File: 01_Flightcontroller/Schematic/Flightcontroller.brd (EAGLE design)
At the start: 63.5 x 61.9 mm, 89 parts, among them IC1 FT232RL, IC2 MPU6000, IC3 BMP280, J1 2908-05WB-MG, U1 STM32F7X2RXT, U2 ATMEGA328P_TQFP, U3 LM3940IMPX-3.3/NOPB, U4 TXB0104, Y1 8MHz, Y2 16MHz

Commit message: Richtiges routen hilfe durch bruno
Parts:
- moved GY87 29.2 mm to (19.1, 91.4)
- moved SONIC1 29.2 mm to (39.4, 99.1)
- moved SONIC2 29.2 mm to (39.4, 96.5)
- moved C34 12.0 mm to (-3.81, 64.8), turned to 90 degrees
- moved ISP1 10.2 mm to (52.1, 64.8)
- moved GPS 10.2 mm to (12.7, 99.1)
- moved OSD 10.2 mm to (12.7, 96.5)
- moved C4 8.98 mm to (39.4, 80.0), turned to 90 degrees
- moved C3 8.89 mm to (27.9, 86.4)
- moved LED_STRIPES 8.89 mm to (29.2, 99.1)
- moved C23 8.52 mm to (-1.27, 64.8), turned to 90 degrees
- moved R2 8.03 mm to (49.5, 86.4)
- moved R3 8.03 mm to (49.5, 83.8)
- moved U4 7.41 mm to (49.5, 77.5)
- moved C28 7.41 mm to (54.6, 80.0)
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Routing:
- net GND: track 264.3 -> 570.1 mm, vias 6 -> 7
- net TRIGG1_IN: track 94.5 -> 21.4 mm, vias 3 -> 0
- net VCC: track 289.1 -> 332.4 mm, vias 13 -> 12
- net ECHO1_IN: track 79.3 -> 40.7 mm, vias 2 -> 0
- net VCC_2: track 207.6 -> 245.9 mm
- net TRIGG2_IN: track 48.6 -> 11.7 mm, vias 3 -> 0
- net UART1_TX: track 92.1 -> 59.1 mm, vias 4 -> 2
- net I2C2_SDA: track 65.3 -> 35.4 mm, vias 1 -> 4
- net UART2_TX: track 59.4 -> 30.3 mm
- net SPI2_MISO: track 76.8 -> 47.8 mm, vias 4 -> 1
- net SD1_CK: track 70.2 -> 43.3 mm, vias 5 -> 1
- net LED_TX: track 50.3 -> 24.1 mm, vias 0 -> 2
- net SD1_CMD: track 62.8 -> 37.2 mm, vias 5 -> 1
- net ECHO2_IN: track 33.3 -> 12.4 mm, vias 2 -> 1
- net A_SPI_NSS: track 47.2 -> 27.7 mm, vias 3 -> 1
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- removed copper zone on layer 16, net GND

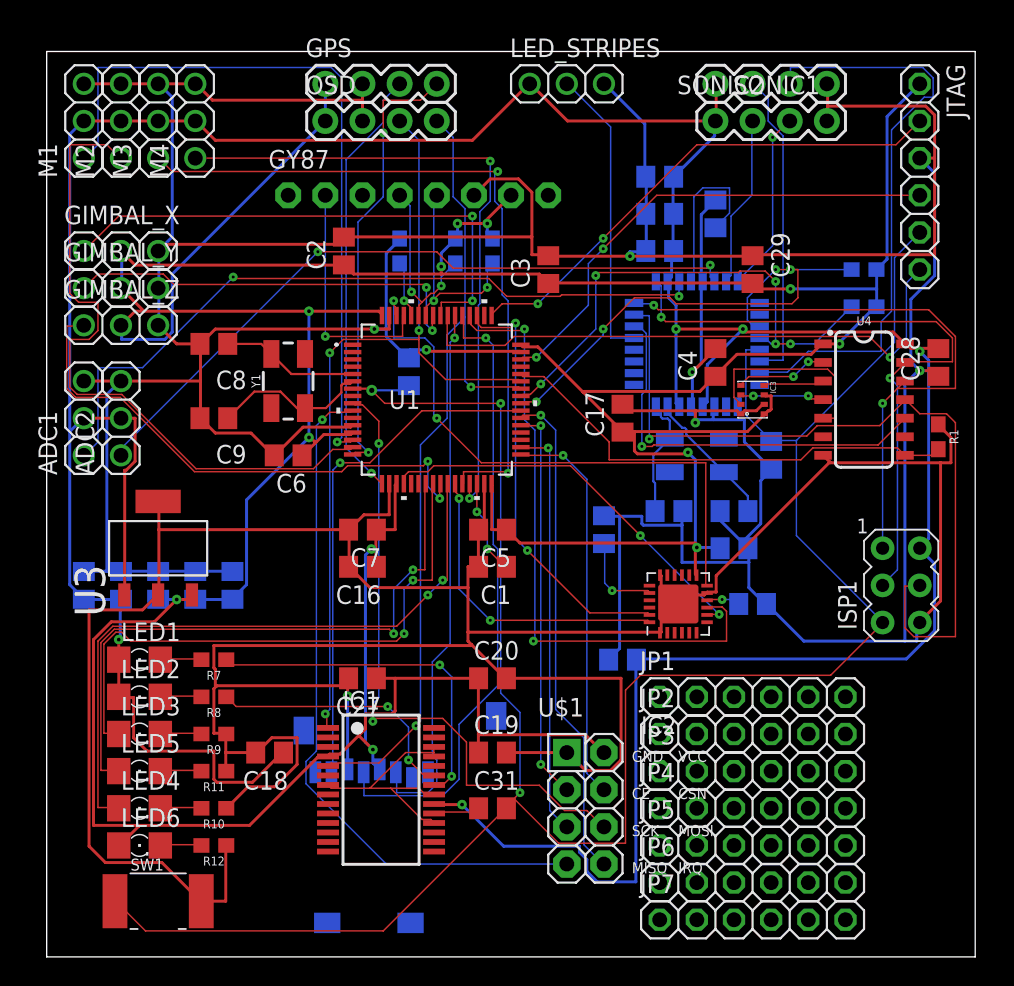
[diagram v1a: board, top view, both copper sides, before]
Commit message: Hinzufügen USB , BATTSENS und VCC/GNDLAYER
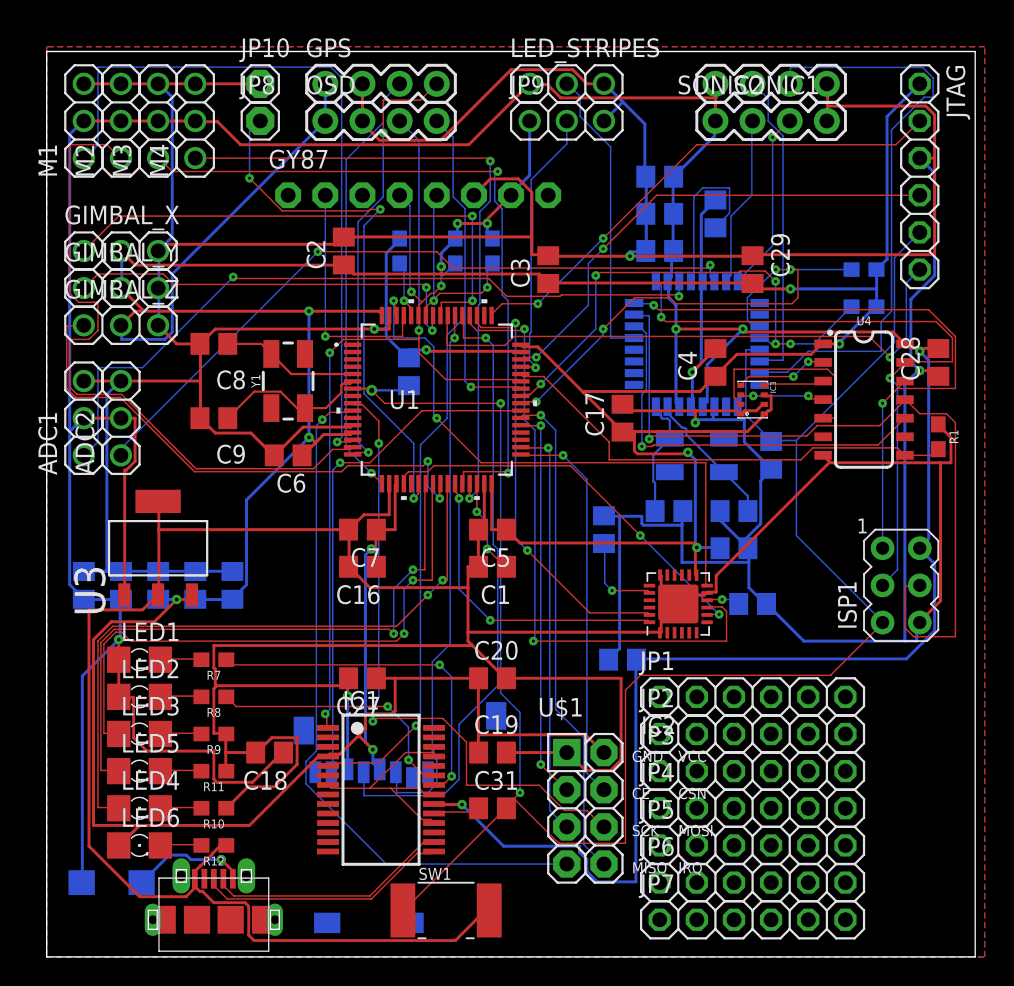
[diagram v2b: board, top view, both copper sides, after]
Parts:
- added D1: (no value), diode:DO214BA
- added JP10, JP8: (no value), adafruit:1X01
- added JP9: (no value), adafruit:1X03
- added U$2: MICRO-USB-RECEPTACLE47589-0001, con-molex-usb:47589-0001
- moved SW1 19.7 mm to (21.0, 42.5)
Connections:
- new net USBDM: IC1.16, U$2.4
- new net USBDP: IC1.15, U$2.3
- new net V_USB: D1.A, U$2.5
- net BATTSENS: now also JP8.1
- net GND: now also JP10.1, JP9.3, U$2.1
- net USBOSD: now also JP9.2
- net VCC: now also JP9.1
- net VCC_2: now also D1.C
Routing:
- net BATTSENS: track 0.00 -> 36.9 mm, vias 0 -> 3
- net GND: track 570.1 -> 605.8 mm
- net RST: track 155.0 -> 133.9 mm
- net USBOSD: track 0.00 -> 19.1 mm, vias 0 -> 1
- net VCC_2: track 245.9 -> 264.2 mm
- net USBDM: track 0.00 -> 17.4 mm
- net USBDP: track 0.00 -> 17.2 mm
- net V_USB: track 0.00 -> 7.99 mm, vias 0 -> 1
- net VCC: track 332.4 -> 337.9 mm
- added copper zone on layer 16, net GND
- added copper zone on layer 1, net VCC

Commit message: Finnishing Board up. BOM
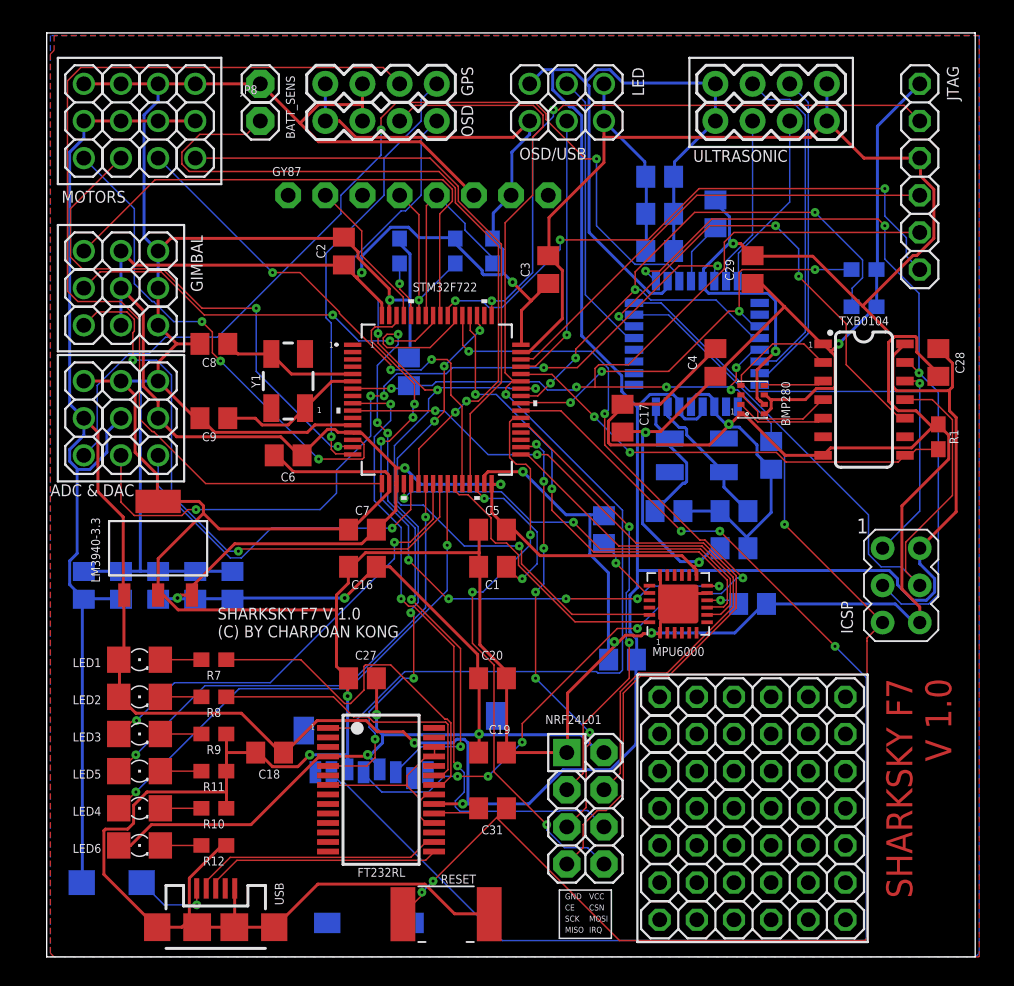
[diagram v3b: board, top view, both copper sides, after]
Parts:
- removed SW1: (no value), adafruit:BTN_CK_KSS
- removed U$2: MICRO-USB-RECEPTACLE47589-0001, con-molex-usb:47589-0001
- added DAC: (no value), adafruit:1X03
- added RESET: (no value), adafruit:BTN_CK_KSS
- added USB: (no value), SparkFun-Connectors:USB-MICROB
- C23: value 1uF -> 10uF
- renumbered IC1 to FT232RL, IC2 to MPU6000, IC3 to BMP280, ISP1 to ICSP, J1 to SD_CARD, JP10 to BATT_SENS, JP9 to OSD/USB, LED_STRIPES to LED, U$1 to NRF24L01, U1 to STM32F722, U2 to ATMEGA328P, U3 to LM3940-3.3, U4 to TXB0104
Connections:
- net DAC_OUT: now also DAC.1
- net GND: now also DAC.3, RESET.P$2, USB.GND, USB.MT1, USB.MT2, USB.P$1, USB.P$2; no longer SW1.P$2, U$2.1
- net RST: now also RESET.P$1; no longer SW1.P$1
- net USBDM: now also USB.D-; no longer U$2.4
- net USBDP: now also USB.D+; no longer U$2.3
- net VCC: now also DAC.2
- net V_USB: now also USB.VBUS; no longer U$2.5
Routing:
- net SD1_D0: track 35.3 -> 90.5 mm, vias 1 -> 3
- net GND: track 605.8 -> 552.8 mm, vias 7 -> 9
- net VCC: track 337.9 -> 292.5 mm
- net UART2_RX: track 29.9 -> 68.8 mm, vias 1 -> 0
- net DAC_OUT: track 0.00 -> 24.5 mm, vias 0 -> 1
- net SD1_CK: track 43.3 -> 64.6 mm, vias 1 -> 7
- net VCC_2: track 264.2 -> 285.3 mm, vias 5 -> 2
- net UART1_RX: track 56.6 -> 76.5 mm, vias 3 -> 2
- net ECHO1_IN: track 40.7 -> 22.0 mm
- net PWM_1: track 49.7 -> 33.4 mm, vias 1 -> 3
- net BATTSENS: track 36.9 -> 50.6 mm, vias 3 -> 2
- net PWM_3: track 48.7 -> 35.2 mm, vias 2 -> 3
- net ADC1: track 50.4 -> 63.4 mm
- net PWM_2: track 45.9 -> 35.4 mm, vias 0 -> 2
- net SPI2_NSS: track 27.0 -> 37.3 mm, vias 1 -> 0
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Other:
- board size 63.5 x 61.9 mm -> 63.5 x 63.2 mm
- board text added: "1"
- board text added: "3V3"
- board text added: "5V"
- board text added: "5V 3V3"
- board text added: "ADC & DAC"
- board text added: "DRDY"
- board text added: "ECHO"
- board text added: "FSYNC"
- board text added: "GIMBAL"
- board text added: "GND"
- board text added: "INT"
- board text added: "MISO"
- board text added: "MOSI"
- board text added: "MOTORS"
- board text added: "RST"
- board text added: "RX"
- board text added: "SCL"
- board text added: "SCLK"
- board text added: "SDA"
- board text added: "SENS"
- board text added: "SHARKSKY F7 V 1.0"
- board text added: "SHARKSKY F7 V 1.0 (C) BY CHARPOAN KONG"
- board text added: "SIG"
- board text added: "SWCLK"
- board text added: "SWDIO"
- board text added: "SWO"
- board text added: "TRG"
- board text added: "TX"
- board text added: "ULTRASONIC"
- board text added: "VCC"
